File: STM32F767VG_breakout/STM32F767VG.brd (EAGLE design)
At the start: 89.8 x 43.8 mm, 42 parts, among them IC1 STM32F767VGT6, IC2 L7805CV, IC3 LD117AS33TR, X4 8MHz, X5 32.768kHz

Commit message: First complete routing
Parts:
- moved LED1 57.6 mm to (24.8, 29.2)
- moved R3 52.9 mm to (22.9, 48.9), turned to 0 degrees
- moved LED3 24.8 mm to (22.2, 29.2), flipped to the top, turned to 270 degrees
- moved R1 23.3 mm to (65.4, 40.0), turned to 180 degrees
- moved R6 23.1 mm to (13.3, 28.6), flipped to the top
- moved D3 21.2 mm to (19.7, 29.2), flipped to the top, turned to 270 degrees
- moved C5 18.8 mm to (31.8, 48.3), flipped to the bottom, turned to 225 degrees
- moved PWR1 9.92 mm to (12.1, 36.8), turned to 180 degrees
- moved BT1 7.75 mm to (13.3, 33.0)
- moved VBAT1 7.24 mm to (13.3, 40.6)
- moved BEAD3 6.29 mm to (48.9, 34.9)
- moved R7 5.85 mm to (17.8, 48.9)
- moved C13 5.08 mm to (48.9, 31.1)
- moved C11 3.81 mm to (36.8, 42.5)
- moved JTAG1 2.01 mm to (68.6, 43.8)
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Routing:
- net GND: track 185.1 -> 280.7 mm, vias 3 -> 6
- net VDD: track 144.9 -> 221.7 mm, vias 2 -> 6
- net PD15: track 34.8 -> 80.4 mm, vias 0 -> 1
- net SWO: track 0.00 -> 40.3 mm, vias 0 -> 1
- net NRST: track 29.8 -> 65.9 mm, vias 0 -> 1
- net PB9: track 0.00 -> 35.3 mm
- net TCK: track 0.00 -> 32.7 mm, vias 0 -> 1
- net BOOT0: track 13.9 -> 45.9 mm, vias 1 -> 2
- net TMS: track 0.00 -> 30.1 mm, vias 0 -> 1
- net N$26: track 2.71 -> 20.5 mm, vias 0 -> 1
- net 5V: track 32.0 -> 16.5 mm
- net N$13: track 31.4 -> 43.5 mm, vias 0 -> 2
- net N$17: track 9.48 -> 20.2 mm
- net MDC: track 57.3 -> 67.1 mm
- net PE5: track 42.0 -> 32.8 mm
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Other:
- board size 89.8 x 43.8 mm -> 89.2 x 41.9 mm

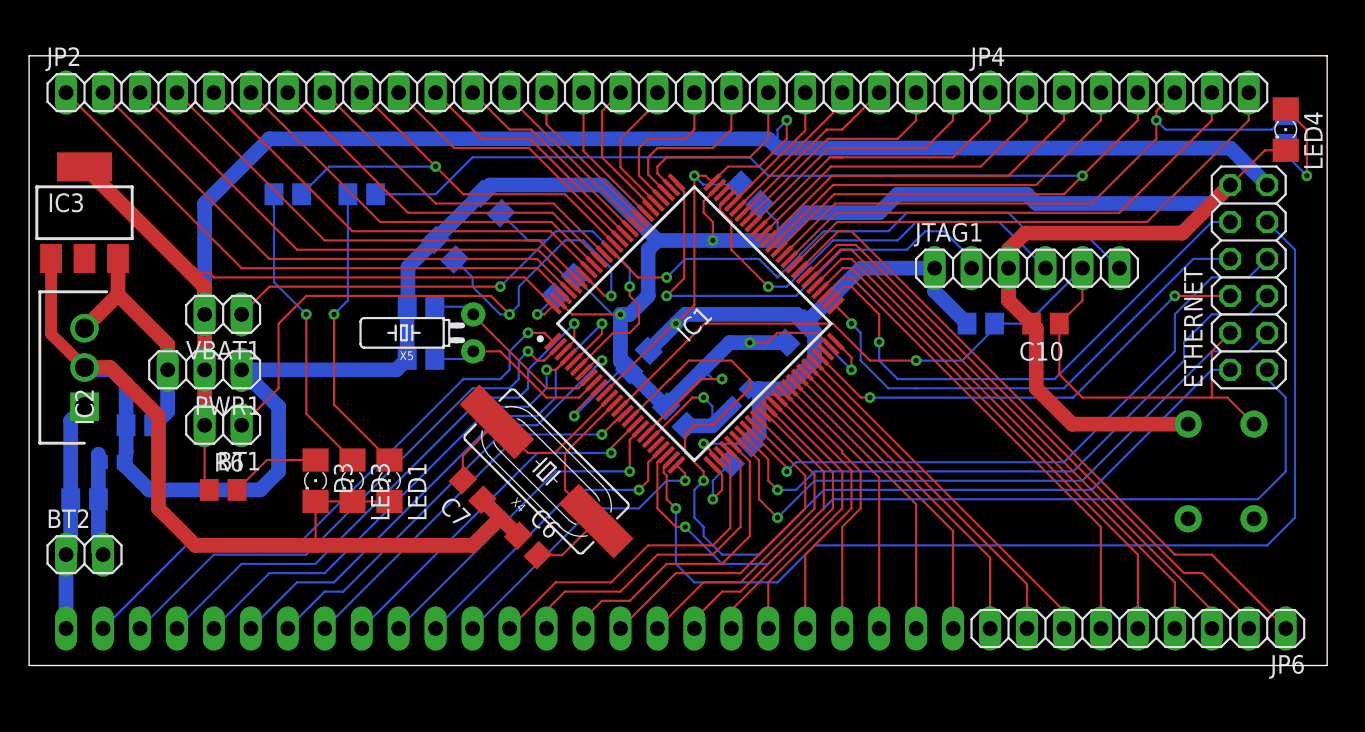
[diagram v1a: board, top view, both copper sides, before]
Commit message: May 1 Feedback Incorporated
Fixed the irregularity and added more space between traces and the pads
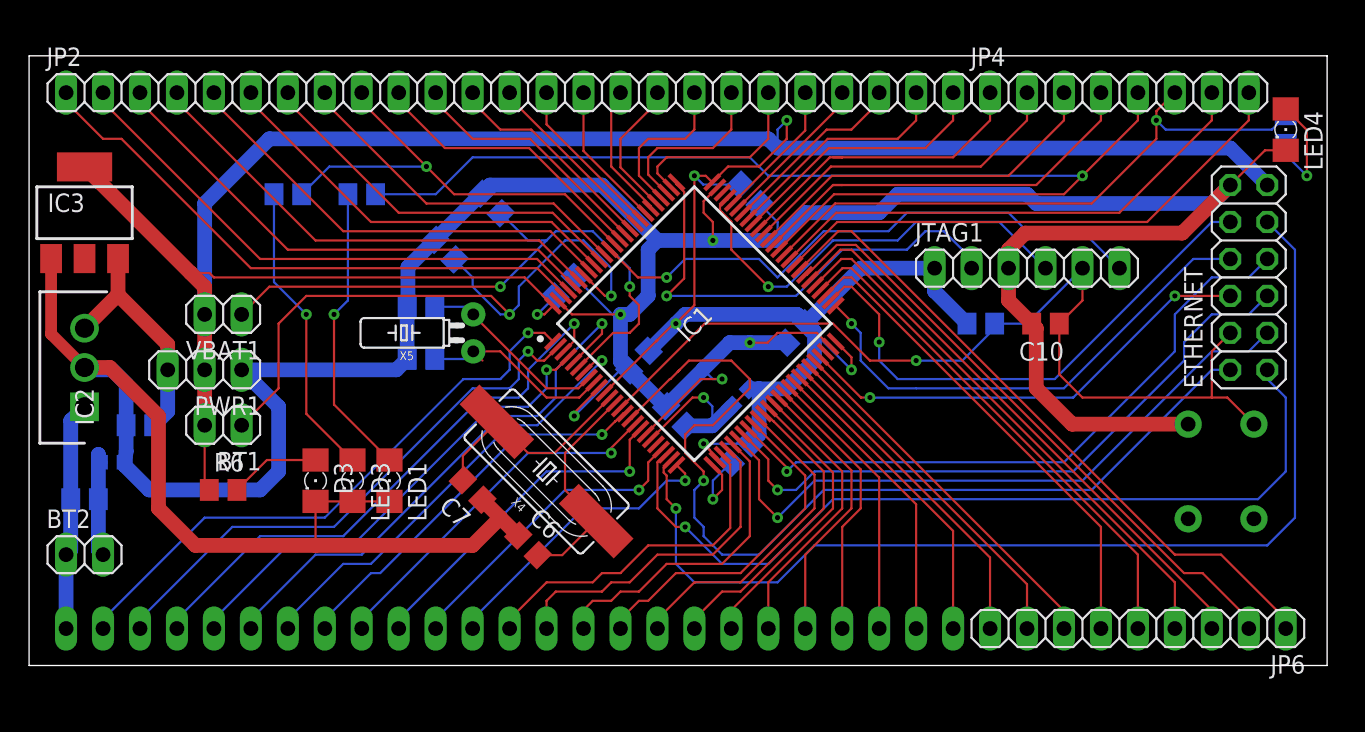
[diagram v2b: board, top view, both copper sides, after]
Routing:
- net PD0: track 9.84 -> 9.32 mm

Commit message: May 1 part 2
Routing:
- net NINT: track 58.9 -> 53.7 mm
- net MDIO: track 73.7 -> 68.9 mm
- net GND: track 280.7 -> 276.6 mm
- net NRST: track 65.9 -> 63.8 mm
- net MDC: track 67.1 -> 69.0 mm
- net TXD1: track 36.8 -> 35.4 mm
- net TXEN: track 32.2 -> 33.3 mm
- net TXD0: track 34.4 -> 35.4 mm
- net RXD1: track 44.6 -> 45.6 mm
- net MGND: track 7.55 -> 6.53 mm
- net RXD0: track 44.7 -> 45.6 mm

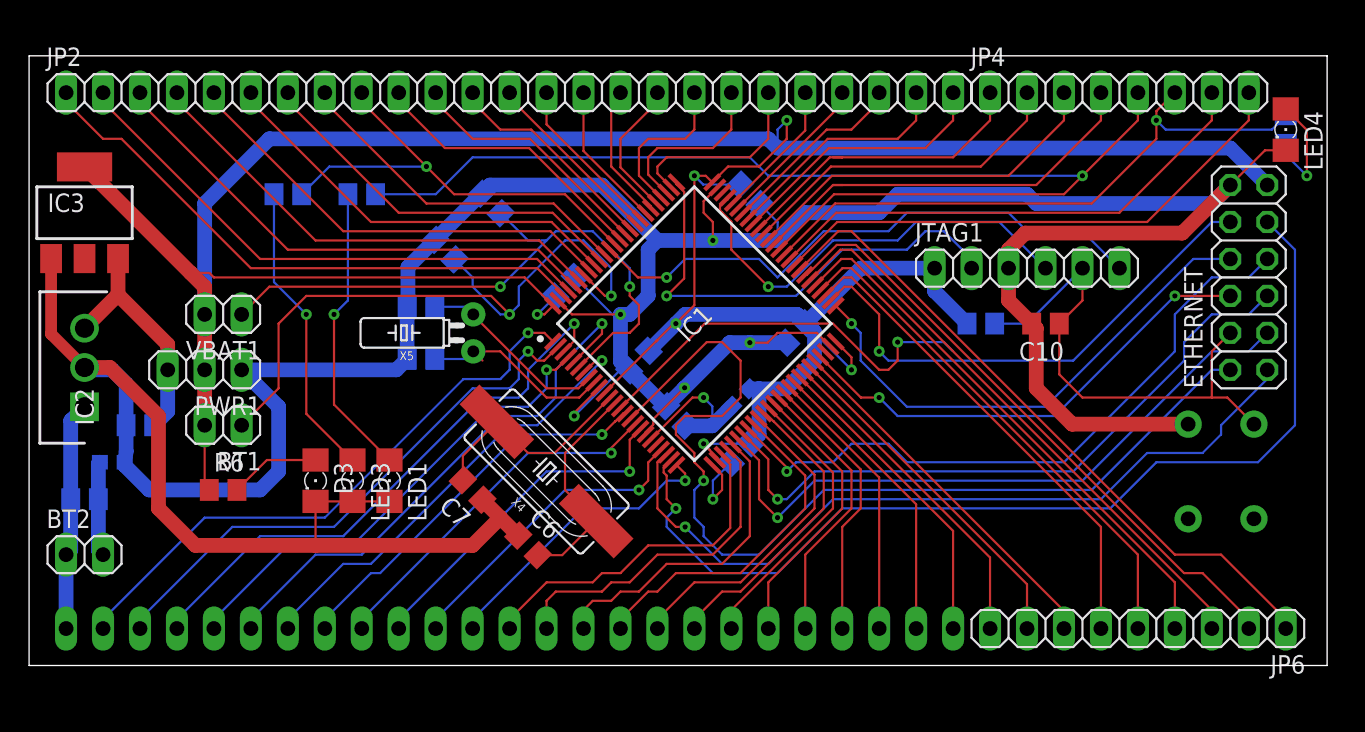
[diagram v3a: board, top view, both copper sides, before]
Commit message: May 2 part 2
Cap connection changed
Same length applied
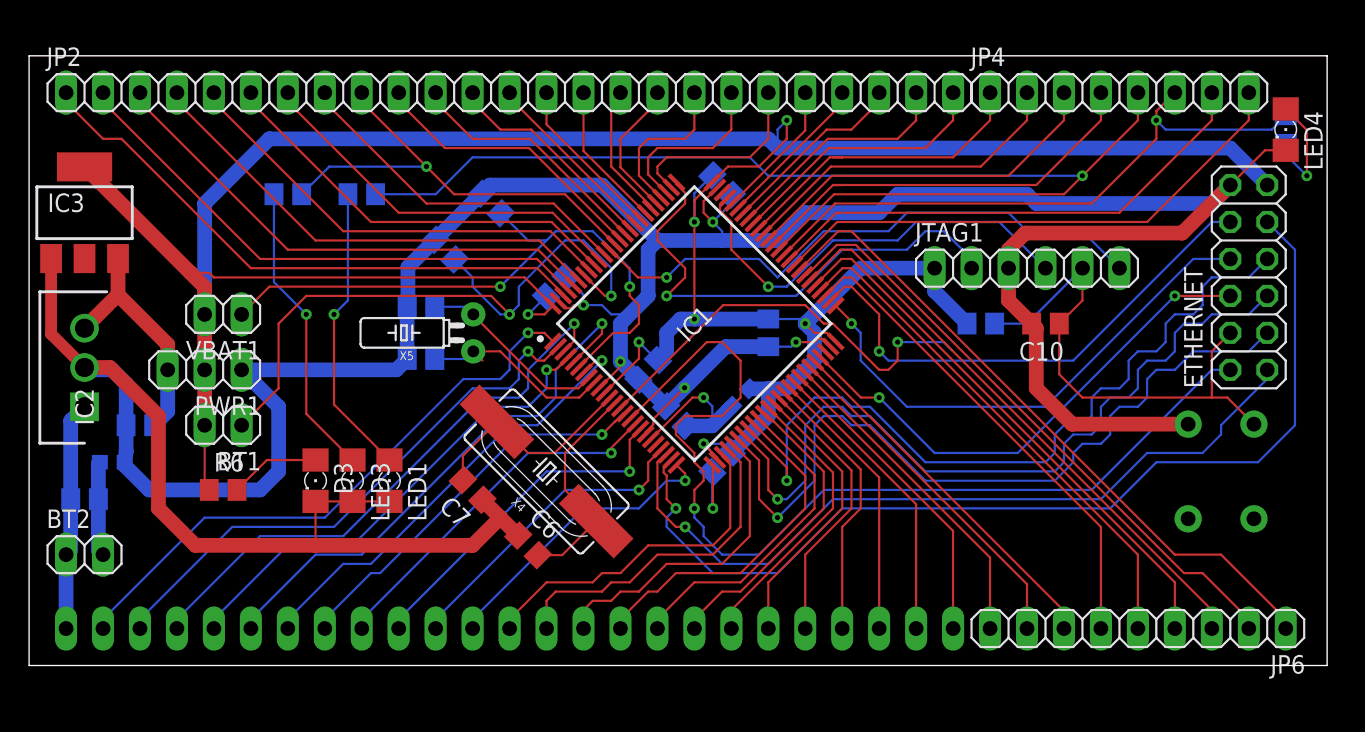
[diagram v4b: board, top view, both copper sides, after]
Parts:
- moved C1 2.01 mm to (47.6, 49.5)
- moved C14 1.91 mm to (50.8, 39.4), turned to 270 degrees
- moved C13 1.42 mm to (47.6, 30.5)
- moved C12 0.90 mm to (42.5, 36.8)
- moved C11 0.63 mm to (36.2, 42.5)
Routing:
- net GND: track 276.6 -> 265.4 mm
- net CRS_DV: track 45.4 -> 53.8 mm
- net RXD0: track 45.6 -> 53.8 mm
- net RXD1: track 45.6 -> 53.6 mm
- net VDD: track 221.7 -> 216.0 mm, vias 6 -> 7
- net TXEN: track 33.3 -> 35.4 mm
- net TCK: track 32.7 -> 34.4 mm
- net NRST: track 63.8 -> 64.8 mm

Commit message: part 3
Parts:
- moved C12 2.69 mm to (40.6, 34.9)
- moved C15 0.90 mm to (45.1, 34.3)
- moved C14 0.64 mm to (51.4, 39.4)
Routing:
- net GND: track 265.4 -> 277.1 mm, vias 6 -> 7
- net AVDD: track 10.7 -> 6.51 mm

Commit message: part x
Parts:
- moved C12 0.90 mm to (41.3, 34.3)
- moved C15 0.90 mm to (45.7, 34.9)
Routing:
- net GND: track 277.1 -> 273.3 mm, vias 7 -> 5
- net VDD: track 215.5 -> 213.9 mm
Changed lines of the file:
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@@
 <attribute name="SPICEPREFIX" value="C" x="36.195" y="42.545" size="1.778" layer="28" rot="MR135" display="off"/>
 </element>
-<element name="C12" library="eagle-ltspice" library_urn="urn:adsk.eagle:library:217" package="C0805" package3d_urn="urn:adsk.eagle:package:13265/1" value="100nF" x="40.64" y="34.925" rot="MR315">
-<attribute name="SPICEMODEL" value="NONE" x="40.64" y="34.925" size="1.778" layer="28" rot="MR315" display="off"/>
-<attribute name="SPICEPREFIX" value="C" x="40.64" y="34.925" size="1.778" layer="28" rot="MR315" display="off"/>
+<element name="C12" library="eagle-ltspice" library_urn="urn:adsk.eagle:library:217" package="C0805" package3d_urn="urn:adsk.eagle:package:13265/1" value="100nF" x="41.275" y="34.29" rot="MR315">
+<attribute name="SPICEMODEL" value="NONE" x="41.275" y="34.29" size="1.778" layer="28" rot="MR315" display="off"/>
+<attribute name="SPICEPREFIX" value="C" x="41.275" y="34.29" size="1.778" layer="28" rot="MR315" display="off"/>
 </element>
 <element name="C13" library="eagle-ltspice" library_urn="urn:adsk.eagle:library:217" package="C0805" package3d_urn="urn:adsk.eagle:package:13265/1" value="100nF" x="47.625" y="30.48" rot="MR315">
@@
 <attribute name="SPICEPREFIX" value="C" x="51.435" y="39.37" size="1.778" layer="28" rot="MR270" display="off"/>
 </element>
-<element name="C15" library="eagle-ltspice" library_urn="urn:adsk.eagle:library:217" package="C0805" package3d_urn="urn:adsk.eagle:package:13265/1" value="100nF" x="45.085" y="34.29" rot="MR45">
-<attribute name="SPICEMODEL" value="NONE" x="45.085" y="34.29" size="1.778" layer="28" rot="MR45" display="off"/>
-<attribute name="SPICEPREFIX" value="C" x="45.085" y="34.29" size="1.778" layer="28" rot="MR45" display="off"/>
+<element name="C15" library="eagle-ltspice" library_urn="urn:adsk.eagle:library:217" package="C0805" package3d_urn="urn:adsk.eagle:package:13265/1" value="100nF" x="45.72" y="34.925" rot="MR45">
+<attribute name="SPICEMODEL" value="NONE" x="45.72" y="34.925" size="1.778" layer="28" rot="MR45" display="off"/>
+<attribute name="SPICEPREFIX" value="C" x="45.72" y="34.925" size="1.778" layer="28" rot="MR45" display="off"/>
 </element>
 <element name="C16" library="eagle-ltspice" library_urn="urn:adsk.eagle:library:217" package="C0805" package3d_urn="urn:adsk.eagle:package:13265/1" value="1uF" x="3.81" y="27.94" rot="MR0">
@@
 <contactref element="IC1" pad="99"/>
 <contactref element="IC2" pad="2"/>
-<wire x1="43.704746875" y1="34.32675" x2="44.41325" y2="34.96175" width="1.016" layer="16"/>
+<wire x1="43.704746875" y1="34.32675" x2="45.04825" y2="35.59675" width="1.016" layer="16"/>
 <wire x1="67.31" y1="41.595" x2="68.9" y2="40.005" width="1.016" layer="1"/>
 <wire x1="67.31" y1="41.595" x2="67.31" y2="43.815" width="1.016" layer="1"/>
@@
 <wire x1="52.705" y1="38.735" x2="52.39" y2="38.42" width="0.1524" layer="16"/>
 <wire x1="51.435" y1="38.42" x2="52.39" y2="38.42" width="0.1524" layer="16"/>
-<wire x1="44.41325" y1="34.96175" x2="47.8715" y2="38.42" width="1.016" layer="16"/>
+<wire x1="45.04825" y1="35.59675" x2="47.8715" y2="38.42" width="1.016" layer="16"/>
 <wire x1="47.8715" y1="38.42" x2="51.435" y2="38.42" width="1.016" layer="16"/>
-<wire x1="39.187746875" y1="35.594065625" x2="40.64" y2="37.04631875" width="0.1524" layer="1"/>
-<wire x1="40.64" y1="37.391496875" x2="40.64" y2="37.04631875" width="0.1524" layer="1"/>
-<via x="40.64" y="37.391496875" extent="1-16" drill="0.35"/>
 <wire x1="36.866753125" y1="43.21675" x2="38.1" y2="41.983503125" width="0.1524" layer="16"/>
-<wire x1="38.1" y1="41.983503125" x2="38.1" y2="41.275" width="0.1524" layer="16"/>
+<wire x1="38.1" y1="41.275" x2="38.1" y2="41.983503125" width="0.1524" layer="16"/>
 <via x="38.1" y="41.275" extent="1-16" drill="0.35"/>
 <wire x1="37.23350625" y1="41.0595" x2="37.44900625" y2="41.275" width="0.1524" layer="1"/>
@@
 <wire x1="36.887321875" y1="41.0595" x2="37.23350625" y2="41.0595" width="0.1524" layer="1"/>
 <wire x1="38.1" y1="41.275" x2="39.37" y2="41.275" width="0.1524" layer="16"/>
-<wire x1="39.37" y1="41.275" x2="40.005" y2="40.64" width="0.1524" layer="16"/>
+<wire x1="40.005" y1="40.64" x2="39.37" y2="41.275" width="0.1524" layer="16"/>
 <wire x1="40.005" y1="40.64" x2="40.64" y2="40.64" width="0.1524" layer="16"/>
 <wire x1="40.9575" y1="40.3225" x2="42.545" y2="41.91" width="1.016" layer="16"/>
 <wire x1="40.9575" y1="40.3225" x2="40.64" y2="40.005" width="1.016" layer="16"/>
-<wire x1="40.64" y1="40.005" x2="40.64" y2="37.391496875" width="1.016" layer="16"/>
 <wire x1="40.64" y1="40.64" x2="40.9575" y2="40.3225" width="0.1524" layer="16"/>
-<wire x1="38.063246875" y1="34.253246875" x2="39.96825" y2="34.253246875" width="0.1524" layer="16"/>
-<wire x1="38.063246875" y1="34.253246875" x2="37.465" y2="33.655" width="0.1524" layer="16"/>
-<via x="37.465" y="33.655" extent="1-16" drill="0.35"/>
-<wire x1="37.465" y1="33.87131875" x2="37.465" y2="33.655" width="0.1524" layer="1"/>
-<wire x1="37.465" y1="33.87131875" x2="39.187746875" y2="35.594065625" width="0.1524" layer="1"/>
-<wire x1="39.96825" y1="34.253246875" x2="40.041753125" y2="34.253246875" width="1.016" layer="16"/>
-<wire x1="41.275" y1="33.02" x2="40.041753125" y2="34.253246875" width="1.016" layer="16"/>
-<wire x1="41.275" y1="33.02" x2="42.4715" y2="33.02" width="1.016" layer="16"/>
-<wire x1="42.4715" y1="33.02" x2="43.46075" y2="34.00925" width="1.016" layer="16"/>
-<wire x1="43.46075" y1="34.00925" x2="44.41325" y2="34.96175" width="1.016" layer="16"/>
+<wire x1="45.04825" y1="35.59675" x2="43.46075" y2="34.00925" width="1.016" layer="16"/>
 <wire x1="46.95325" y1="29.808246875" x2="46.391753125" y2="29.808246875" width="1.016" layer="16"/>
-<wire x1="46.391753125" y1="29.808246875" x2="45.72" y2="30.48" width="1.016" layer="16"/>
-<wire x1="45.72" y1="30.48" x2="43.815" y2="30.48" width="1.016" layer="16"/>
-<wire x1="43.815" y1="30.48" x2="41.275" y2="33.02" width="1.016" layer="16"/>
+<wire x1="45.72" y1="30.48" x2="46.391753125" y2="29.808246875" width="1.016" layer="16"/>
 <wire x1="46.355" y1="47.625" x2="46.355" y2="48.418175" width="0.1524" layer="1"/>
 <wire x1="47.06350625" y1="47.625" x2="46.355" y2="47.625" width="0.1524" layer="16"/>
@@
 <wire x1="43.46075" y1="33.503109375" x2="43.46075" y2="34.00925" width="0.1524" layer="1"/>
 <via x="43.46075" y="34.00925" extent="1-16" drill="0.35"/>
+<wire x1="40.64" y1="36.83" x2="40.005" y2="36.195" width="1.016" layer="16"/>
+<wire x1="40.005" y1="36.195" x2="40.005" y2="34.29" width="1.016" layer="16"/>
+<wire x1="40.005" y1="34.29" x2="40.60325" y2="33.69175" width="1.016" layer="16"/>
+<wire x1="40.60325" y1="33.69175" x2="40.60325" y2="33.618246875" width="1.016" layer="16"/>
+<wire x1="40.64" y1="40.005" x2="40.64" y2="36.83" width="1.016" layer="16"/>
+<wire x1="41.87325" y1="32.348246875" x2="40.60325" y2="33.618246875" width="1.016" layer="16"/>
+<wire x1="41.87325" y1="32.348246875" x2="43.741496875" y2="30.48" width="1.016" layer="16"/>
+<wire x1="43.741496875" y1="30.48" x2="45.72" y2="30.48" width="1.016" layer="16"/>
+<wire x1="41.87325" y1="32.42175" x2="41.87325" y2="32.348246875" width="1.016" layer="16"/>
+<wire x1="43.46075" y1="34.00925" x2="41.87325" y2="32.42175" width="1.016" layer="16"/>
+<wire x1="40.005" y1="36.195" x2="39.187746875" y2="35.594065625" width="0" layer="19" extent="1-16"/>
 </signal>
 <signal name="VDD">
@@
 <wire x1="57.150003125" y1="43.815" x2="53.340003125" y2="40.005" width="1.016" layer="16"/>
 <wire x1="53.340003125" y1="40.005" x2="53.34" y2="40.005" width="1.016" layer="16"/>
-<wire x1="41.311753125" y1="35.59675" x2="42.451515625" y2="36.7365125" width="0.1524" layer="16"/>
+<wire x1="41.946753125" y1="34.96175" x2="42.451515625" y2="36.7365125" width="0" layer="19" extent="1-16"/>
 <wire x1="42.451515625" y1="36.7365125" x2="42.451515625" y2="36.923484375" width="0.1524" layer="16"/>
 <via x="42.451515625" y="36.923484375" extent="1-16" drill="0.35"/>
@@
 <via x="44.45" y="33.02" extent="1-16" drill="0.35"/>
 <wire x1="44.45" y1="33.02" x2="45.15850625" y2="33.02" width="0.1524" layer="16"/>
-<wire x1="45.15850625" y1="33.02" x2="45.756753125" y2="33.618246875" width="0.1524" layer="16"/>
-<wire x1="45.756753125" y1="33.618246875" x2="47.58825" y2="33.618246875" width="1.016" layer="16"/>
-<wire x1="47.58825" y1="33.618246875" x2="48.293959375" y2="34.32395625" width="1.016" layer="16"/>
+<wire x1="46.391753125" y1="34.253246875" x2="46.4624625" y2="34.32395625" width="1.016" layer="16"/>
+<wire x1="46.4624625" y1="34.32395625" x2="48.293959375" y2="34.32395625" width="1.016" layer="16"/>
+<wire x1="45.15850625" y1="33.02" x2="46.391753125" y2="34.253246875" width="0.1524" layer="16"/>
 </signal>
 <signal name="12V">
@@
 <wire x1="45.72" y1="31.115" x2="45.085" y2="31.75" width="0.1524" layer="1"/>
 <wire x1="45.085" y1="32.385" x2="45.085" y2="31.75" width="0.1524" layer="1"/>
-<wire x1="47.625" y1="33.655" x2="46.355" y2="33.655" width="0.1524" layer="1"/>
-<wire x1="46.355" y1="33.655" x2="45.085" y2="32.385" width="0.1524" layer="1"/>
+<wire x1="45.085" y1="32.385" x2="46.355" y2="33.655" width="0.1524" layer="1"/>
 <wire x1="47.625" y1="33.655" x2="50.165" y2="36.195" width="0.1524" layer="1"/>
 <wire x1="50.165" y1="36.195" x2="50.165" y2="36.83" width="0.1524" layer="1"/>
 <wire x1="50.165" y1="36.83" x2="48.26" y2="38.735" width="0.1524" layer="1"/>
 <wire x1="48.26" y1="38.735" x2="46.57131875" y2="38.735" width="0.1524" layer="1"/>
+<wire x1="46.355" y1="33.655" x2="47.625" y2="33.655" width="0.1524" layer="1"/>
 </signal>
 <signal name="NINT">

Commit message: polygon added
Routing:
- net GND: track 273.3 -> 276.2 mm, vias 5 -> 42
- net VDD: track 213.9 -> 211.7 mm, vias 7 -> 8
- net PC10: track 12.0 -> 10.9 mm
- net PA15: track 13.4 -> 12.3 mm
- net SWO: track 40.3 -> 39.3 mm
- net PC11: track 10.9 -> 10.2 mm
- added copper zone on layer 1, net GND
- added copper zone on layer 16, net GND
